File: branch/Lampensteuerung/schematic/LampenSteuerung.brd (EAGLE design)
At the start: 41.2 x 33.8 mm, 47 parts, among them IC1 LM358D, IC2 TSOP34836, IC4 TS2951-3.0, Q1 BCR135, Q2 BCR135, Q3 BCR135, Q4 BCW60SMD, T1 SFH320, X2 MKDSN1,5/5-5,08

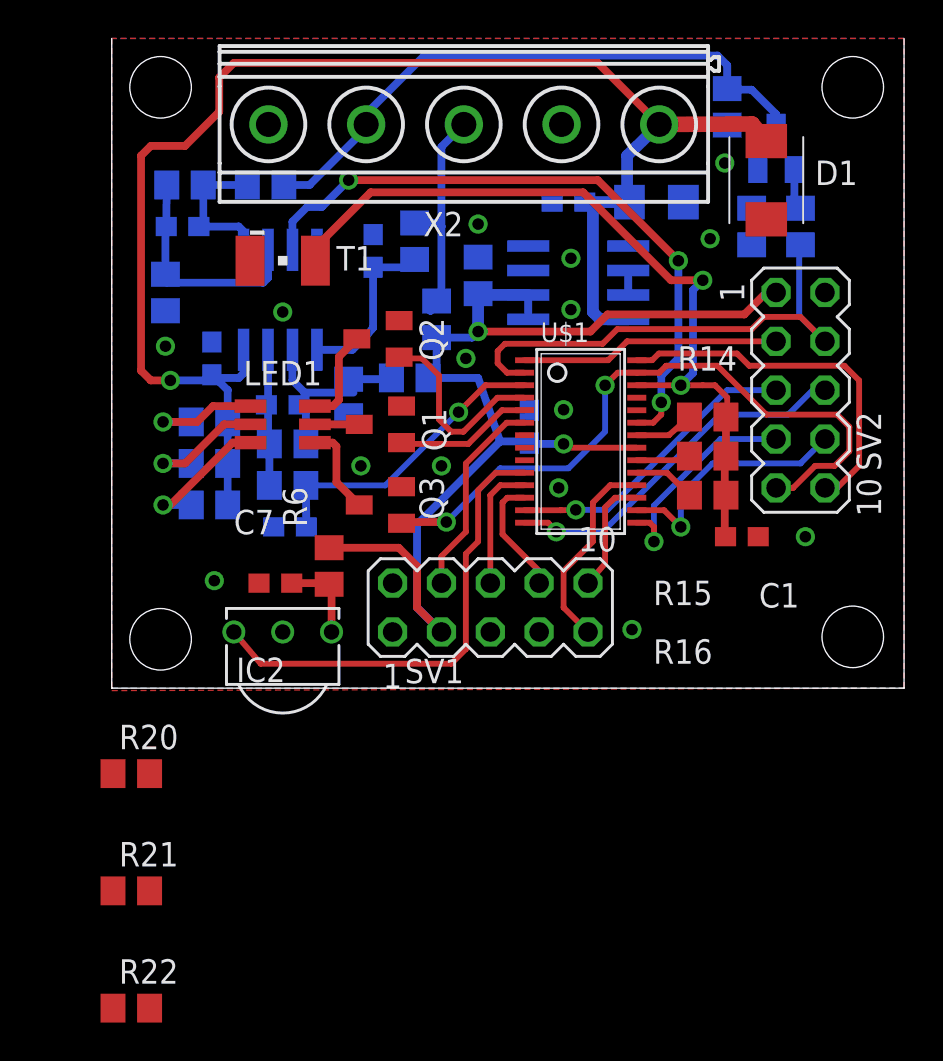
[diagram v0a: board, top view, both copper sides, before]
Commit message: added missing pull-up resistors added wire pads for output shifted some components slightly to ease mounting
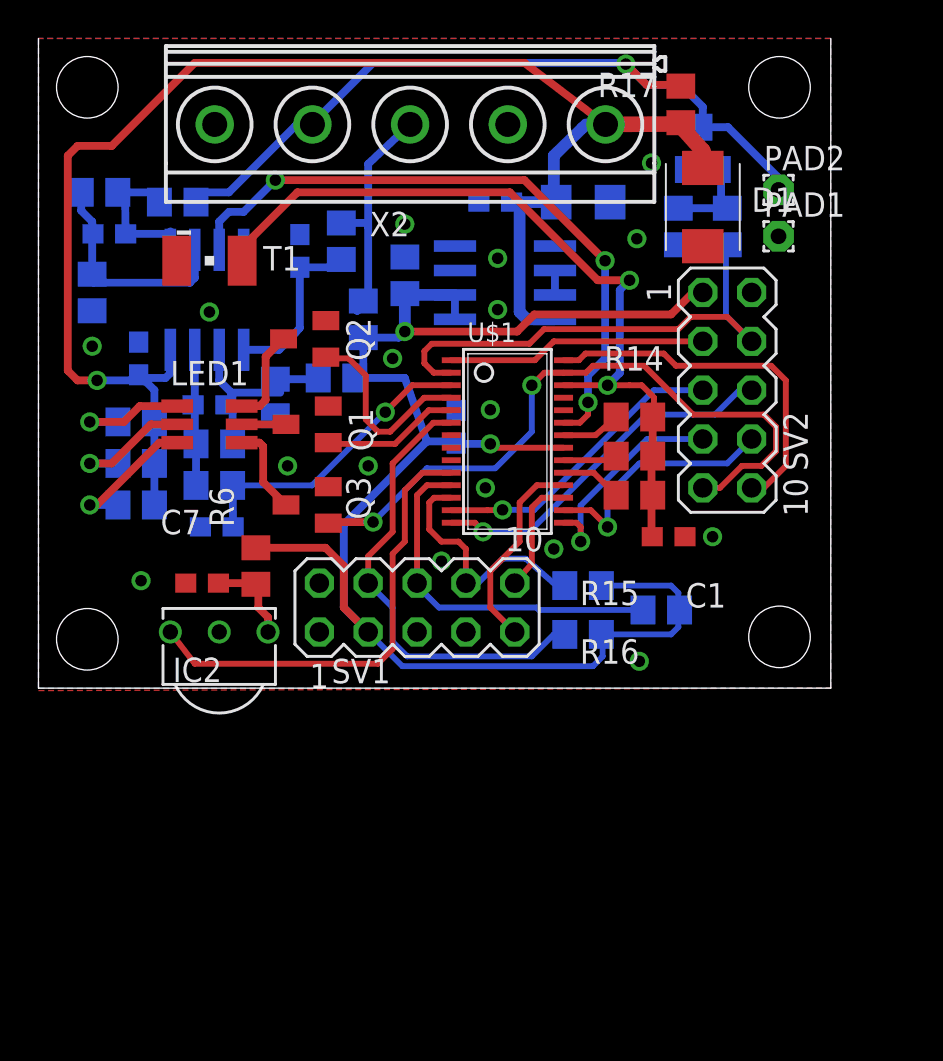
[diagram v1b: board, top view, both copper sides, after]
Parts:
- added PAD1: GND, wirepad:1,6/0,8
- added PAD2: Out, wirepad:1,6/0,8
- moved R21 31.2 mm to (32.4, 4.06), flipped to the bottom, turned to 180 degrees
- moved R22 30.5 mm to (28.3, 2.79), flipped to the bottom, turned to 180 degrees
- moved R20 25.4 mm to (28.3, 5.33), flipped to the bottom, turned to 180 degrees
- moved R4 4.66 mm to (7.24, 25.3)
- moved R1 4.46 mm to (3.17, 25.8)
- moved C4 3.83 mm to (3.68, 23.6)
- moved C1 3.81 mm to (32.8, 7.87)
- moved C2 3.81 mm to (21.7, 13.6)
- moved C8 3.81 mm to (23.7, 25.3)
- moved Q4 3.81 mm to (34.5, 28.1)
- moved R10 3.81 mm to (16.9, 19.2)
- moved R14 3.81 mm to (31.0, 14.1)
- moved R15 3.81 mm to (31.0, 12.1)
- moved R16 3.81 mm to (31.0, 10.0)
- moved R18 3.81 mm to (35.8, 24.0)
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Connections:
- net GND: now also PAD1.1
- net N$9: now also PAD2.1
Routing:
- net +UB: track 61.5 -> 85.8 mm
- net N$13: track 10.7 -> 24.0 mm
- net N$16: track 6.57 -> 19.0 mm
- net N$9: track 31.5 -> 40.6 mm, vias 0 -> 1
- net N$15: track 6.23 -> 13.0 mm
- net +12V: track 81.7 -> 79.6 mm
